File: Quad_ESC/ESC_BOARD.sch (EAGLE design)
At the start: 33 parts, among them U1 SN74CBTLV3257PWR, Y1 ECS-80-S-4X

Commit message: Labeling
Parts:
- removed RSH1: 1 mΩ, INA4181A4:CSS2H-2512
- C10: value 4.7uF -> 100nF
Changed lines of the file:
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@@
 <part name="GND10" library="supply2" library_urn="urn:adsk.eagle:library:372" deviceset="GND" device=""/>
 <part name="U$8" library="PI_Shield_Library" deviceset="TCAN337D" device=""/>
-<part name="C10" library="SparkFun-Capacitors" library_urn="urn:adsk.eagle:library:510" deviceset="4.7UF" device="0603" package3d_urn="urn:adsk.eagle:package:37414/1" value="4.7uF"/>
+<part name="C10" library="SparkFun-Capacitors" library_urn="urn:adsk.eagle:library:510" deviceset="4.7UF" device="0603" package3d_urn="urn:adsk.eagle:package:37414/1" value="100nF"/>
 <part name="+3V3" library="supply1" library_urn="urn:adsk.eagle:library:371" deviceset="+3V3" device=""/>
 <part name="U$4" library="PI_Shield_Library" deviceset="STM32F042K6T6" device=""/>
@@
 <part name="P+7" library="supply1" library_urn="urn:adsk.eagle:library:371" deviceset="+12V" device=""/>
 <part name="P+8" library="supply1" library_urn="urn:adsk.eagle:library:371" deviceset="+12V" device=""/>
-<part name="RSH1" library="INA4181A4" deviceset="CSS2H-2512" device="" value="1 mΩ"/>
 </parts>
 <sheets>
@@
 <instance part="P+7" gate="1" x="195.58" y="50.8"/>
 <instance part="P+8" gate="1" x="259.08" y="50.8"/>
-<instance part="RSH1" gate="G$1" x="330.2" y="190.5"/>
 </instances>
 <busses>

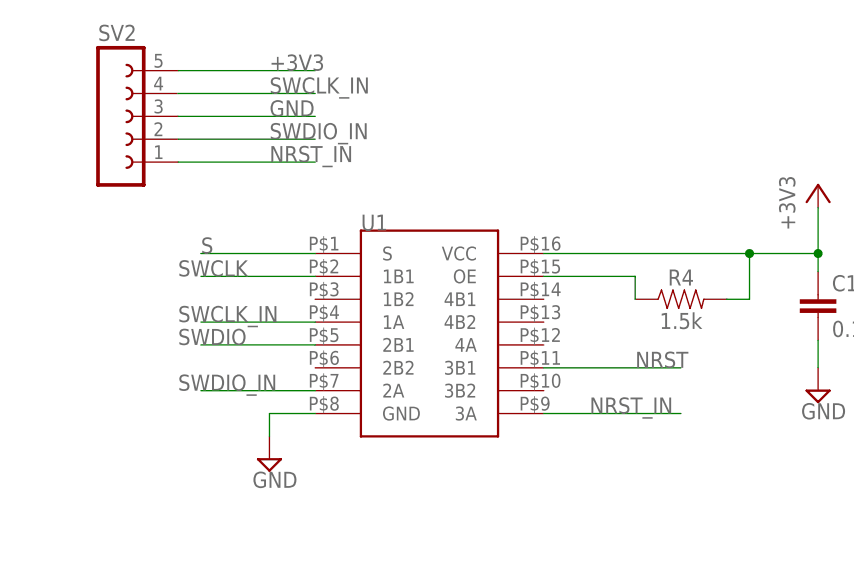
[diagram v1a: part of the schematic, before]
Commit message: fixed mux and manufacturing errors
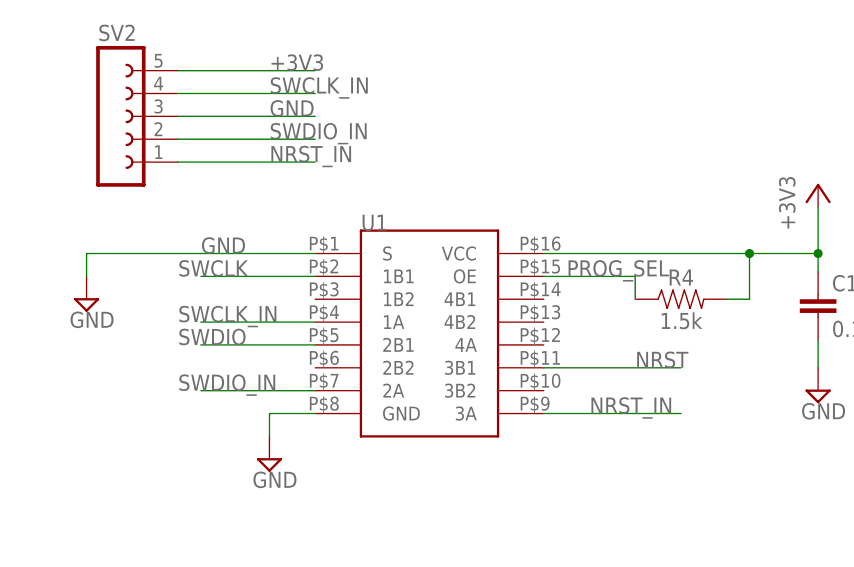
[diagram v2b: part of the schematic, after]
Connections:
- removed net N$4: R4.1, U1.OE
- removed net S: U1.S
- net GND: now also U1.S
- net PROG_SEL: now also R4.1, U1.OE
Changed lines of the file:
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@@
 <?xml version="1.0" encoding="utf-8"?>
 <!DOCTYPE eagle SYSTEM "eagle.dtd">
-<eagle version="8.6.1">
+<eagle version="9.1.3">
 <drawing>
 <settings>
@@
 <part name="P+7" library="supply1" library_urn="urn:adsk.eagle:library:371" deviceset="+12V" device=""/>
 <part name="P+8" library="supply1" library_urn="urn:adsk.eagle:library:371" deviceset="+12V" device=""/>
+<part name="GND13" library="supply2" library_urn="urn:adsk.eagle:library:372" deviceset="GND" device=""/>
 </parts>
 <sheets>
@@
 <instance part="P+7" gate="1" x="195.58" y="50.8"/>
 <instance part="P+8" gate="1" x="259.08" y="50.8"/>
+<instance part="GND13" gate="GND" x="25.4" y="53.34">
+<attribute name="VALUE" x="23.495" y="50.165" size="1.778" layer="96"/>
+</instance>
 </instances>
 <busses>
@@
 <pinref part="GND20" gate="GND" pin="GND"/>
 <wire x1="261.62" y1="71.12" x2="261.62" y2="68.58" width="0.1524" layer="91"/>
+</segment>
+<segment>
+<pinref part="GND13" gate="GND" pin="GND"/>
+<wire x1="25.4" y1="55.88" x2="25.4" y2="58.42" width="0.1524" layer="91"/>
+<pinref part="U1" gate="G$1" pin="S"/>
+<wire x1="50.8" y1="58.42" x2="38.1" y2="58.42" width="0.1524" layer="91"/>
+<label x="38.1" y="58.42" size="1.778" layer="95"/>
+<wire x1="25.4" y1="58.42" x2="38.1" y2="58.42" width="0.1524" layer="91"/>
 </segment>
 </net>
@@
 </segment>
 </net>
-<net name="S" class="0">
-<segment>
-<pinref part="U1" gate="G$1" pin="S"/>
-<wire x1="50.8" y1="58.42" x2="38.1" y2="58.42" width="0.1524" layer="91"/>
-<label x="38.1" y="58.42" size="1.778" layer="95"/>
-</segment>
-</net>
-<net name="N$4" class="0">
+<net name="SWCLK_IN" class="0">
+<segment>
+<pinref part="U1" gate="G$1" pin="1A"/>
+<wire x1="50.8" y1="50.8" x2="38.1" y2="50.8" width="0.1524" layer="91"/>
+<label x="35.56" y="50.8" size="1.778" layer="95"/>
+</segment>
+<segment>
+<pinref part="SV2" gate="G$1" pin="4"/>
+<wire x1="35.56" y1="76.2" x2="50.8" y2="76.2" width="0.1524" layer="91"/>
+<label x="45.72" y="76.2" size="1.778" layer="95"/>
+</segment>
+</net>
+<net name="SWDIO_IN" class="0">
+<segment>
+<pinref part="U1" gate="G$1" pin="2A"/>
+<wire x1="50.8" y1="43.18" x2="38.1" y2="43.18" width="0.1524" layer="91"/>
+<label x="35.56" y="43.18" size="1.778" layer="95"/>
+</segment>
+<segment>
+<pinref part="SV2" gate="G$1" pin="2"/>
+<wire x1="35.56" y1="71.12" x2="50.8" y2="71.12" width="0.1524" layer="91"/>
+<label x="45.72" y="71.12" size="1.778" layer="95"/>
+</segment>
+</net>
+<net name="NRST_IN" class="0">
+<segment>
+<pinref part="U1" gate="G$1" pin="3A"/>
+<wire x1="76.2" y1="40.64" x2="91.44" y2="40.64" width="0.1524" layer="91"/>
+<label x="81.28" y="40.64" size="1.778" layer="95"/>
+</segment>
+<segment>
+<pinref part="SV2" gate="G$1" pin="1"/>
+<wire x1="35.56" y1="68.58" x2="50.8" y2="68.58" width="0.1524" layer="91"/>
+<label x="45.72" y="68.58" size="1.778" layer="95"/>
+</segment>
+</net>
+<net name="PROG_SEL" class="0">
+<segment>
+<pinref part="U$1" gate="G$1" pin="P$5"/>
+<wire x1="210.82" y1="66.04" x2="200.66" y2="66.04" width="0.1524" layer="91"/>
+<label x="198.12" y="66.04" size="1.778" layer="95"/>
+</segment>
 <segment>
 <pinref part="U1" gate="G$1" pin="OE"/>
@@
 <wire x1="76.2" y1="55.88" x2="86.36" y2="55.88" width="0.1524" layer="91"/>
 <wire x1="86.36" y1="55.88" x2="86.36" y2="53.34" width="0.1524" layer="91"/>
-</segment>
-</net>
-<net name="SWCLK_IN" class="0">
-<segment>
-<pinref part="U1" gate="G$1" pin="1A"/>
-<wire x1="50.8" y1="50.8" x2="38.1" y2="50.8" width="0.1524" layer="91"/>
-<label x="35.56" y="50.8" size="1.778" layer="95"/>
-</segment>
-<segment>
-<pinref part="SV2" gate="G$1" pin="4"/>
-<wire x1="35.56" y1="76.2" x2="50.8" y2="76.2" width="0.1524" layer="91"/>
-<label x="45.72" y="76.2" size="1.778" layer="95"/>
-</segment>
-</net>
-<net name="SWDIO_IN" class="0">
-<segment>
-<pinref part="U1" gate="G$1" pin="2A"/>
-<wire x1="50.8" y1="43.18" x2="38.1" y2="43.18" width="0.1524" layer="91"/>
-<label x="35.56" y="43.18" size="1.778" layer="95"/>
-</segment>
-<segment>
-<pinref part="SV2" gate="G$1" pin="2"/>
-<wire x1="35.56" y1="71.12" x2="50.8" y2="71.12" width="0.1524" layer="91"/>
-<label x="45.72" y="71.12" size="1.778" layer="95"/>
-</segment>
-</net>
-<net name="NRST_IN" class="0">
-<segment>
-<pinref part="U1" gate="G$1" pin="3A"/>
-<wire x1="76.2" y1="40.64" x2="91.44" y2="40.64" width="0.1524" layer="91"/>
-<label x="81.28" y="40.64" size="1.778" layer="95"/>
-</segment>
-<segment>
-<pinref part="SV2" gate="G$1" pin="1"/>
-<wire x1="35.56" y1="68.58" x2="50.8" y2="68.58" width="0.1524" layer="91"/>
-<label x="45.72" y="68.58" size="1.778" layer="95"/>
-</segment>
-</net>
-<net name="PROG_SEL" class="0">
-<segment>
-<pinref part="U$1" gate="G$1" pin="P$5"/>
-<wire x1="210.82" y1="66.04" x2="200.66" y2="66.04" width="0.1524" layer="91"/>
-<label x="198.12" y="66.04" size="1.778" layer="95"/>
-</segment>
-</net>
+<label x="78.74" y="55.88" size="1.778" layer="95"/>
+</segment>
+</net>

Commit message: CAD for ESC board
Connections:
- net ESC1_B: now also ESC1_CON.A; no longer ESC1_CON.C
- net ESC1_R: now also ESC1_CON.C; no longer ESC1_CON.A
- net ESC2_B: now also ESC2_CON.A; no longer ESC2_CON.C
- net ESC2_R: now also ESC2_CON.C; no longer ESC2_CON.A

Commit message: cad for connectors to backplane
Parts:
- U$1: device ESC_to_Backplane_Connectors:ESC2BACKPLANE -> ESC_to_Backplane_Connectors_esc:ESC2BACKPLANE
